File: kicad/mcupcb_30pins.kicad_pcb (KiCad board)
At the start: 2 copper layers, 62 x 31 mm, 34 parts, among them J1 Conn_01x30_MountingPin, J2 ICSP, U1 ATmega32U4-AU, Y1 X322516MLB4SI

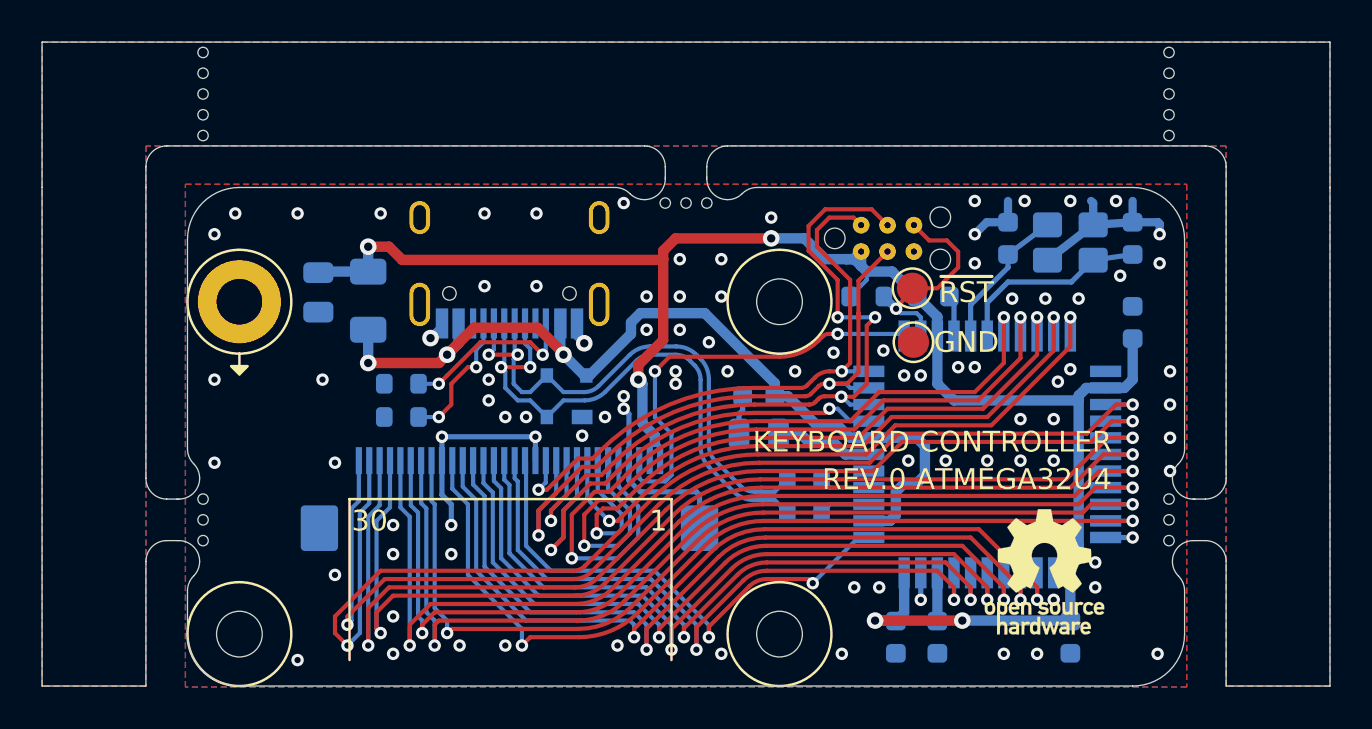
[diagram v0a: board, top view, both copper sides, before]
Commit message: Fixed flipped D+/D-
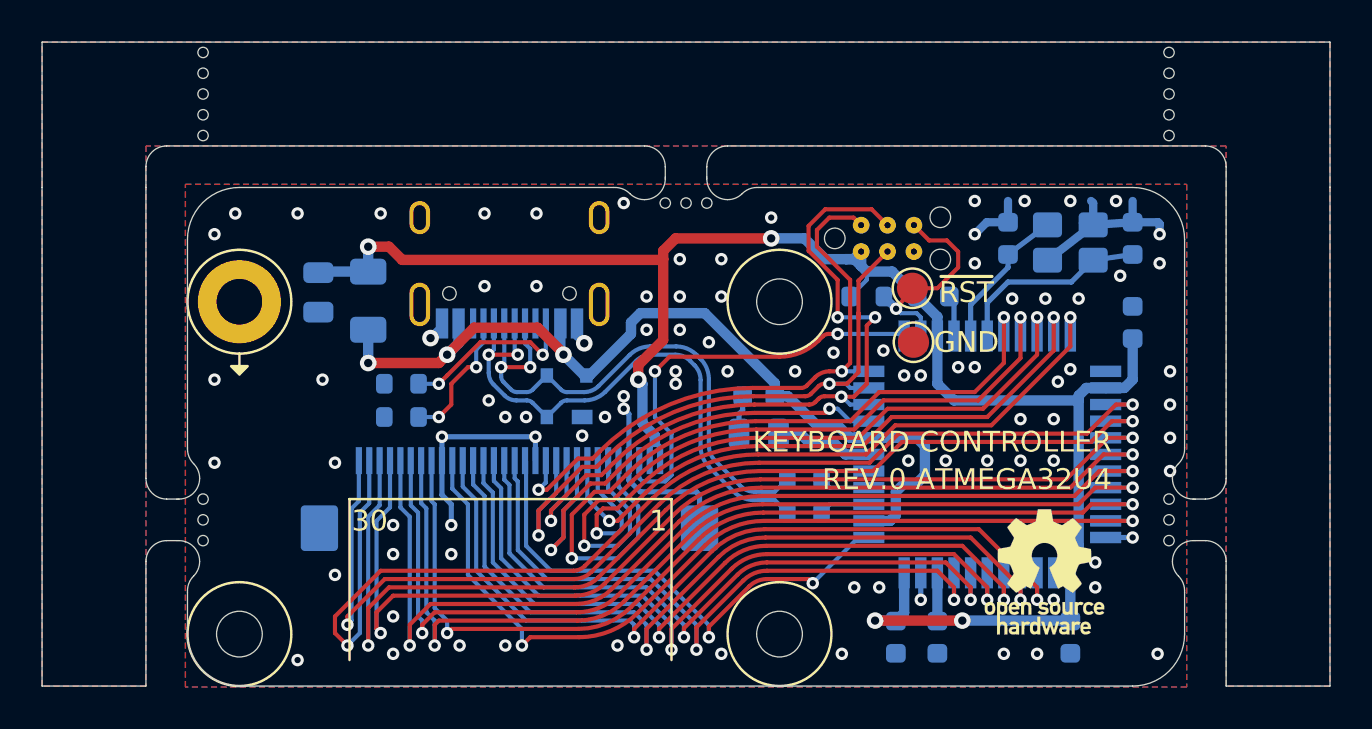
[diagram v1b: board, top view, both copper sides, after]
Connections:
- D1 pad 2: /D+ -> /D-
- D1 pad 3: /D- -> /D+
- R4 pad 2: /D- -> /D+
- R5 pad 2: /D+ -> /D-
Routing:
- net /D-: track 26.2 -> 27.3 mm
- net GND: vias 95 -> 94
